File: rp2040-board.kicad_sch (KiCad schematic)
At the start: 95 parts, among them J1 24V IN, J10 E0-RUNOUT, J11 FAN0, J12 FAN1, J13 FAN2, J14 HB, J15 E0, J16 TH-E0, J2 USB4105-GF-A, J22 Exp. Header 2, J23 Exp. Header 3, J3 PGA2040, J4 Exp. Header 1, J5 PROBE, J6 X-ENDSTOP, J7 TH-HB, J8 Y-ENDSTOP, J9 Z-ENDSTOP, Q1 AO3400C, Q2 AO3400C, Q3 AO3400C, U1 AMS1117-3.3, U2 TPS5450DDAR, U3 74HCT365D,653, U4 FDS8896, U5 FDS8896

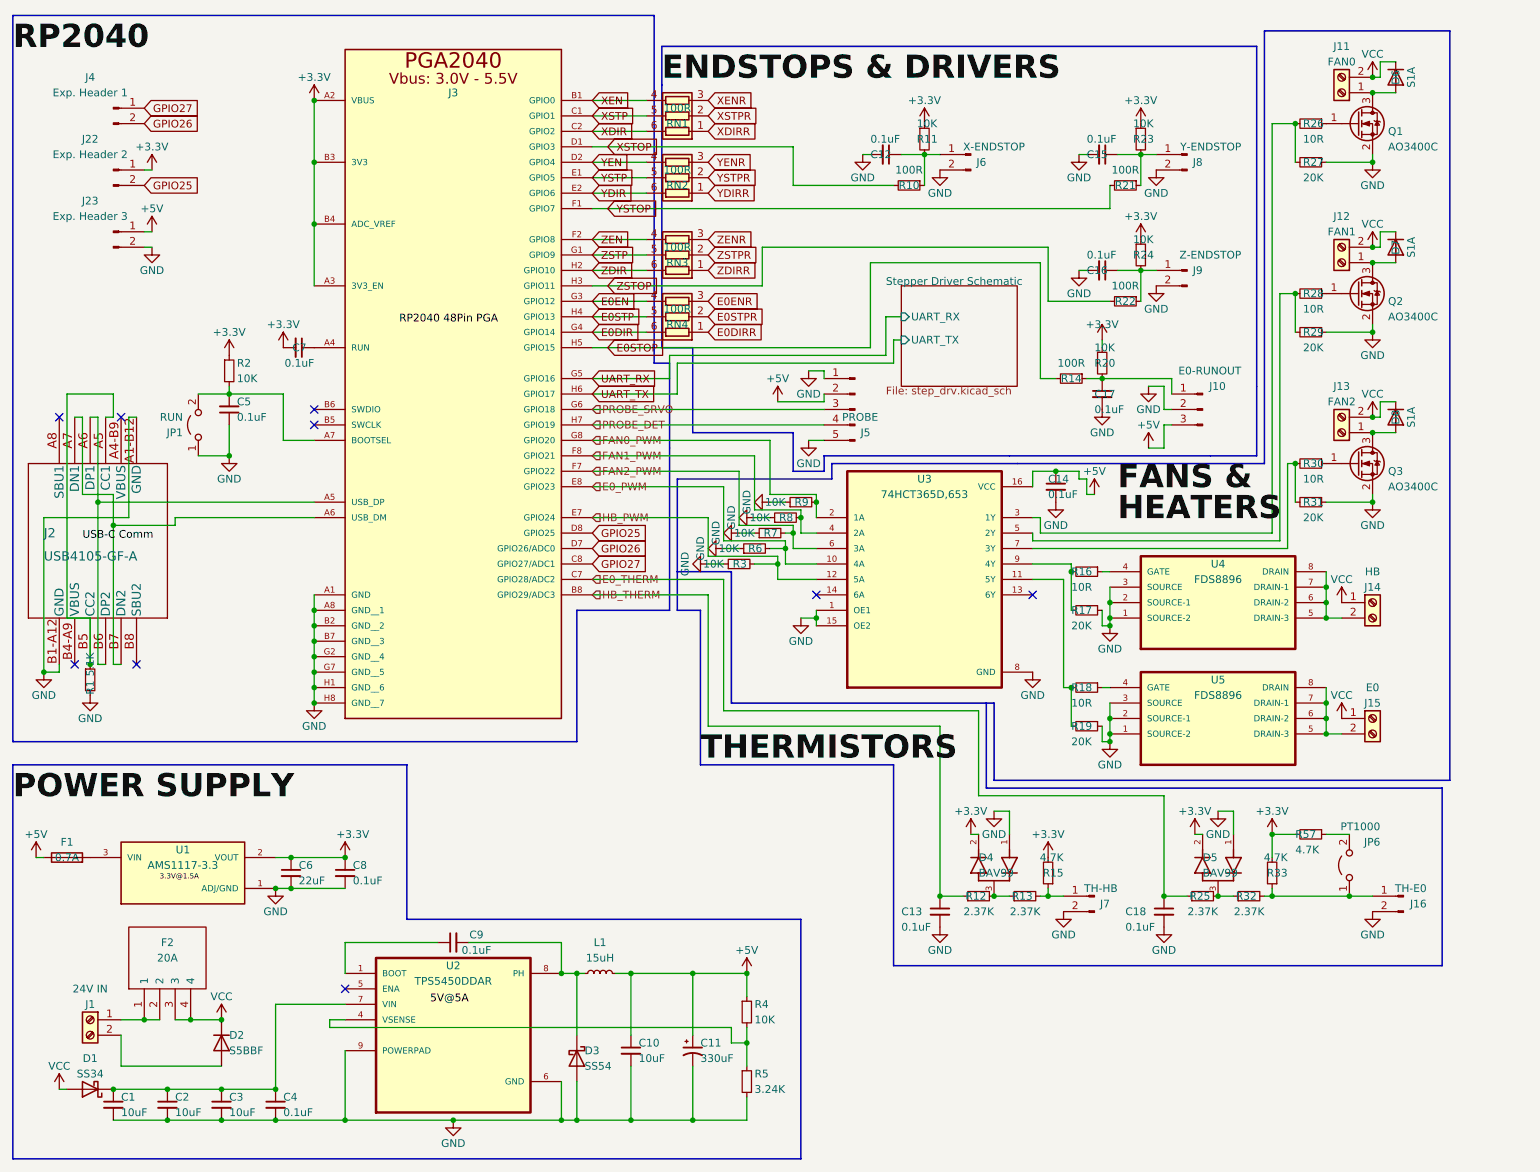
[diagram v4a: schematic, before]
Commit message: Big updates, start of V2, actual RP2040
change from V1.2 to V2 because of many optimizations to come
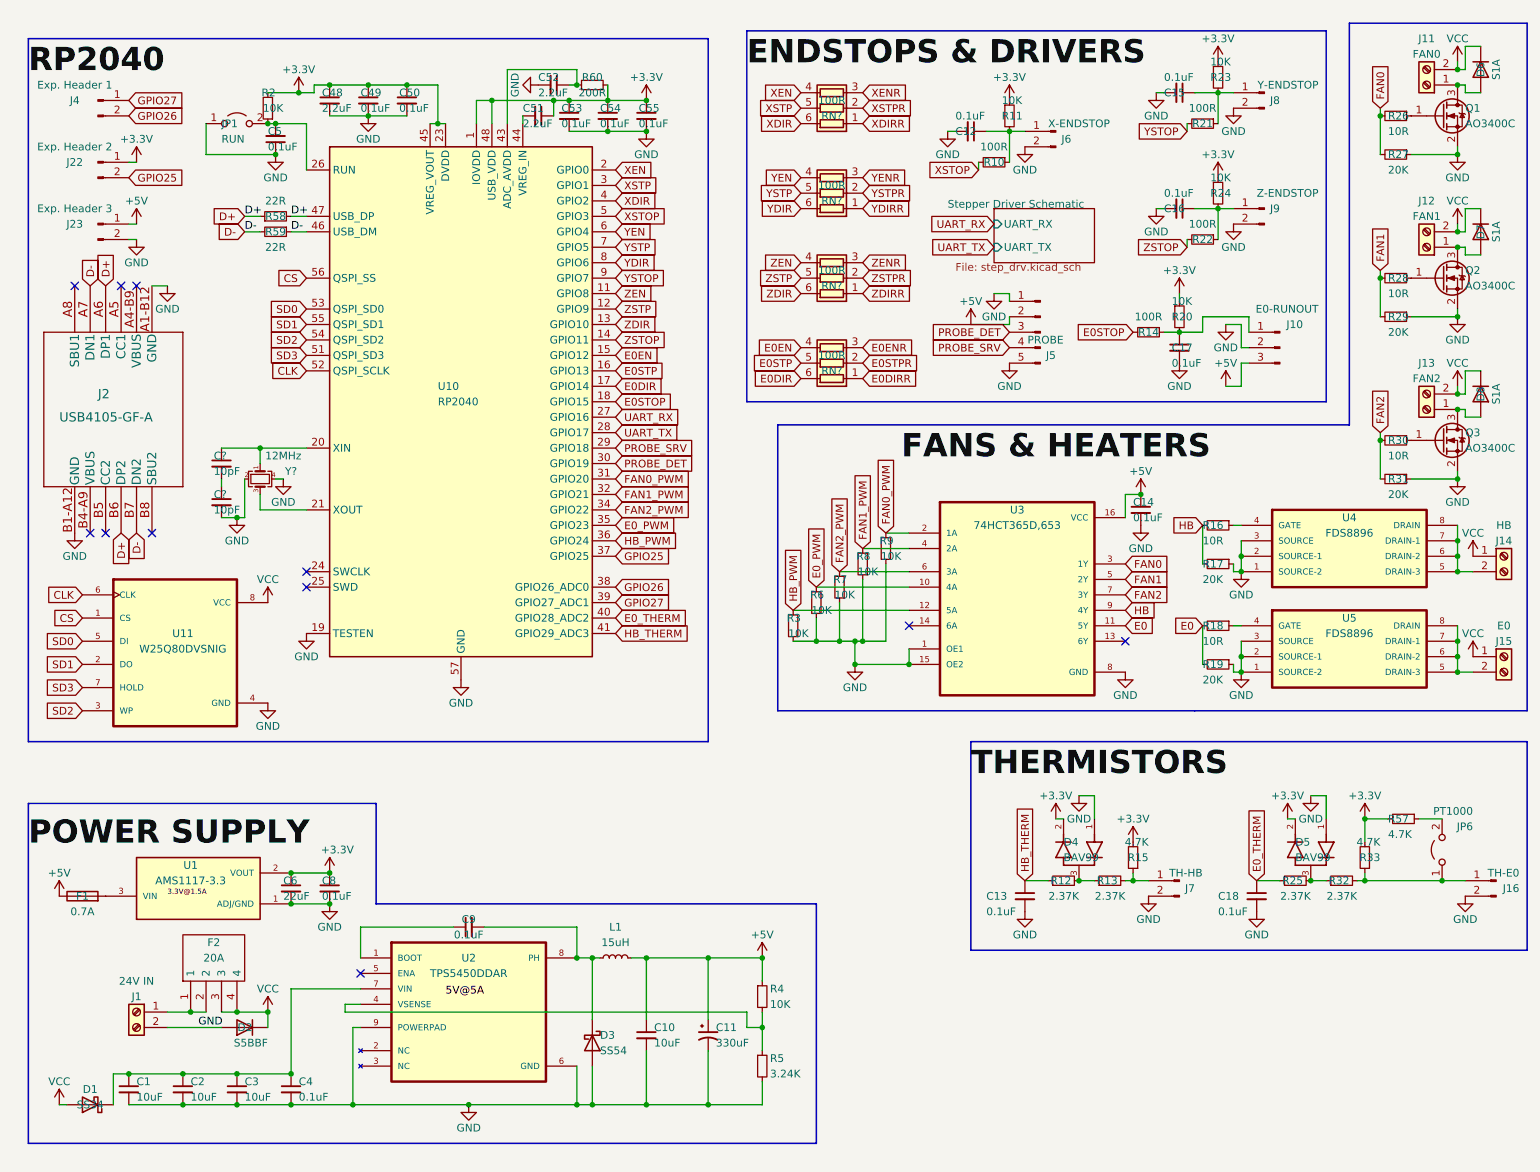
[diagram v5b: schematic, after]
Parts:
- removed C7: 0.1uF, Capacitor_SMD:C_0805_2012Metric_Pad1.18x1.45mm, symbol Device:C_Small
- removed J3: PGA2040, PGA2040:PGA2040_PTH_NO_SLOT, symbol PGA2040:PGA2040
- removed R1: 5.1K, Resistor_SMD:R_0805_2012Metric_Pad1.20x1.40mm, symbol Device:R_Small
- removed RN1, RN2, RN3, RN4: 100R, Resistor_SMD:R_Array_Convex_4x0603, symbol Device:R_Pack03
- added C48, C51, C52: 2.2uF, Capacitor_SMD:C_0805_2012Metric, symbol Device:C_Small
- added C49, C50, C53, C54, C55: 0.1uF, Capacitor_SMD:C_0805_2012Metric, symbol Device:C_Small
- added C? (x2): 10pF, Capacitor_SMD:C_0805_2012Metric, symbol Device:C_Small
- added R58, R59: 22R, Resistor_SMD:R_0805_2012Metric, symbol Device:R_Small
- added R60: 200R, Capacitor_SMD:C_0805_2012Metric, symbol Device:R_Small
- added RN? (x4): 100R, Resistor_SMD:R_Array_Convex_4x0603, symbol Device:R_Pack03
- added U10: RP2040, Package_DFN_QFN:QFN-56-1EP_7x7mm_P0.4mm_EP3.2x3.2mm, symbol MCU_RaspberryPi:RP2040
- added U11: W25Q80DVSNIG, SOIC127P600X175-8N, symbol W25Q80DVSNIG_TR:W25Q80DVSNIG_TR
- added Y?: 12MHz, Oscillator:Oscillator_SMD_SeikoEpson_SG8002CE-4Pin_3.2x2.5mm, symbol Device:Crystal_GND24_Small
- C1, C10, C12, C13, C14, C15, C16, C17, C18, C2, C3, C4, C5, C6, C8, C9: footprint Capacitor_SMD:C_0805_2012Metric_Pad1.18x1.45mm -> Capacitor_SMD:C_0805_2012Metric
- F1: footprint Fuse:Fuse_1812_4532Metric_Pad1.30x3.40mm -> Fuse:Fuse_1812_4532Metric
- L1: footprint Inductor_SMD:L_1210_3225Metric_Pad1.42x2.65mm -> Inductor_SMD:L_1210_3225Metric
- R10, R11, R12, R13, R14, R15, R16, R17, R18, R19, R2, R20, R21, R22, R23, R24, R25, R26, R27, R28, R29, R3, R30, R31, R32, R33, R4, R5, R57, R6, R7, R8, R9: footprint Resistor_SMD:R_0805_2012Metric_Pad1.20x1.40mm -> Resistor_SMD:R_0805_2012Metric
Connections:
- net PROBE_SRVO is gone; now on net PROBE_DET: J5.3 (Pin_3)
- net +3.3V: now also R2.2, C48.1, C49.1, C50.1, C51.1, C53.1, C54.1, C55.1, R60.2, U10.1 (IOVDD), U10.10 (IOVDD), U10.22 (IOVDD), U10.23 (DVDD), U10.33 (IOVDD), U10.42 (IOVDD), U10.45 (VREG_VOUT), U10.48 (USB_VDD), U10.49 (IOVDD), U10.50 (DVDD); no longer R2.1
- net E0DIR: now also RN?.6 (R1.2), U10.17 (GPIO14)
- net E0DIRR: now also RN?.1 (R1.1)
- net E0EN: now also RN?.4 (R3.2), U10.15 (GPIO12)
- net E0ENR: now also RN?.3 (R3.1)
- net E0STOP: now also U10.18 (GPIO15)
- net E0STP: now also RN?.5 (R2.2), U10.16 (GPIO13)
- net E0STPR: now also RN?.2 (R2.1)
- net E0_PWM: now also U10.35 (GPIO23)
- net E0_THERM: now also U10.40 (GPIO28_ADC2)
- net FAN0_PWM: now also U10.31 (GPIO20)
- net FAN1_PWM: now also U10.32 (GPIO21)
- net FAN2_PWM: now also U10.34 (GPIO22)
- net GND: now also D2.1 (A), J1.2 (Pin_2), C48.2, C49.2, C50.2, C52.2, C53.2, C54.2, C55.2, C?.2, U10.19 (TESTEN), U10.57 (GND), U11.4 (GND), Y?.2, Y?.4
- net GPIO25: now also U10.37 (GPIO25)
- net GPIO26: now also U10.38 (GPIO26_ADC0)
- net GPIO27: now also U10.39 (GPIO27_ADC1)
- net HB_PWM: now also U10.36 (GPIO24)
- net HB_THERM: now also U10.41 (GPIO29_ADC3)
- net PROBE_DET: now also U10.30 (GPIO19); no longer J5.4 (Pin_4)
- net UART_RX: now also U10.27 (GPIO16)
- net UART_TX: now also U10.28 (GPIO17)
- net VCC: now also U11.8 (VCC)
- net XDIR: now also RN?.6 (R1.2), U10.4 (GPIO2)
- net XDIRR: now also RN?.1 (R1.1)
- net XEN: now also RN?.4 (R3.2), U10.2 (GPIO0)
- net XENR: now also RN?.3 (R3.1)
- net XSTOP: now also U10.5 (GPIO3)
- net XSTP: now also RN?.5 (R2.2), U10.3 (GPIO1)
- net XSTPR: now also RN?.2 (R2.1)
- net YDIR: now also RN?.6 (R1.2), U10.8 (GPIO6)
- net YDIRR: now also RN?.1 (R1.1)
- net YEN: now also RN?.4 (R3.2), U10.6 (GPIO4)
- net YENR: now also RN?.3 (R3.1)
- net YSTOP: now also U10.9 (GPIO7)
- net YSTP: now also RN?.5 (R2.2), U10.7 (GPIO5)
- net YSTPR: now also RN?.2 (R2.1)
- net ZDIR: now also RN?.6 (R1.2), U10.13 (GPIO10)
- net ZDIRR: now also RN?.1 (R1.1)
- net ZEN: now also RN?.4 (R3.2), U10.11 (GPIO8)
- net ZENR: now also RN?.3 (R3.1)
- net ZSTOP: now also U10.14 (GPIO11)
- net ZSTP: now also RN?.5 (R2.2), U10.12 (GPIO9)
- net ZSTPR: now also RN?.2 (R2.1)
- net E0: now reaches R18.2, R19.2, U3.11 (5Y)
- net at C5.2, JP1.2 (B): now also R2.1, U10.26 (RUN); no longer R2.2
- net FAN0: now reaches R26.2, R27.2, U3.3 (1Y)
- net HB: now reaches R16.2, R17.2, U3.9 (4Y)
- net FAN1: now reaches R28.2, R29.2, U3.5 (2Y)
- net at J2.A5 (CC1): no longer J2.B5 (CC2)
- net D+: now reaches J2.A6 (DP1), J2.B6 (DP2)
- net D+: now also R58.1, R58.2, U10.47 (USB_DP)
- net D-: now reaches J2.A7 (DN1), J2.B7 (DN2)
- net D-: now also R59.1, R59.2, U10.46 (USB_DM)
- net FAN2: now reaches R30.2, R31.2, U3.7 (3Y)
- new net: C?.1, U10.20 (XIN), Y?.1
- new net: U10.21 (XOUT), Y?.3
- new net: C52.1, R60.1, U10.43 (ADC_AVDD)
- new net: C51.2, U10.44 (VREG_IN)
- new net: C?.1, C?.2
- new net CLK: U10.52 (QSPI_SCLK), U11.6 (CLK)
- new net CS: U10.56 (QSPI_SS), U11.1 (CS)
- new net PROBE_SRV: J5.4 (Pin_4), U10.29 (GPIO18)
- new net SD0: U10.53 (QSPI_SD0), U11.5 (DI)
- new net SD1: U10.55 (QSPI_SD1), U11.2 (DO)
- new net SD2: U10.54 (QSPI_SD2), U11.3 (WP)
- new net SD3: U10.51 (QSPI_SD3), U11.7 (HOLD)
- no-connect marks 9 -> 11
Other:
- title: RP2040 Board -> FriedSalmon2040
- moved on the sheet: C1, C10, C11, C12, C13, C14, C15, C16, C17, C18, C2, C3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

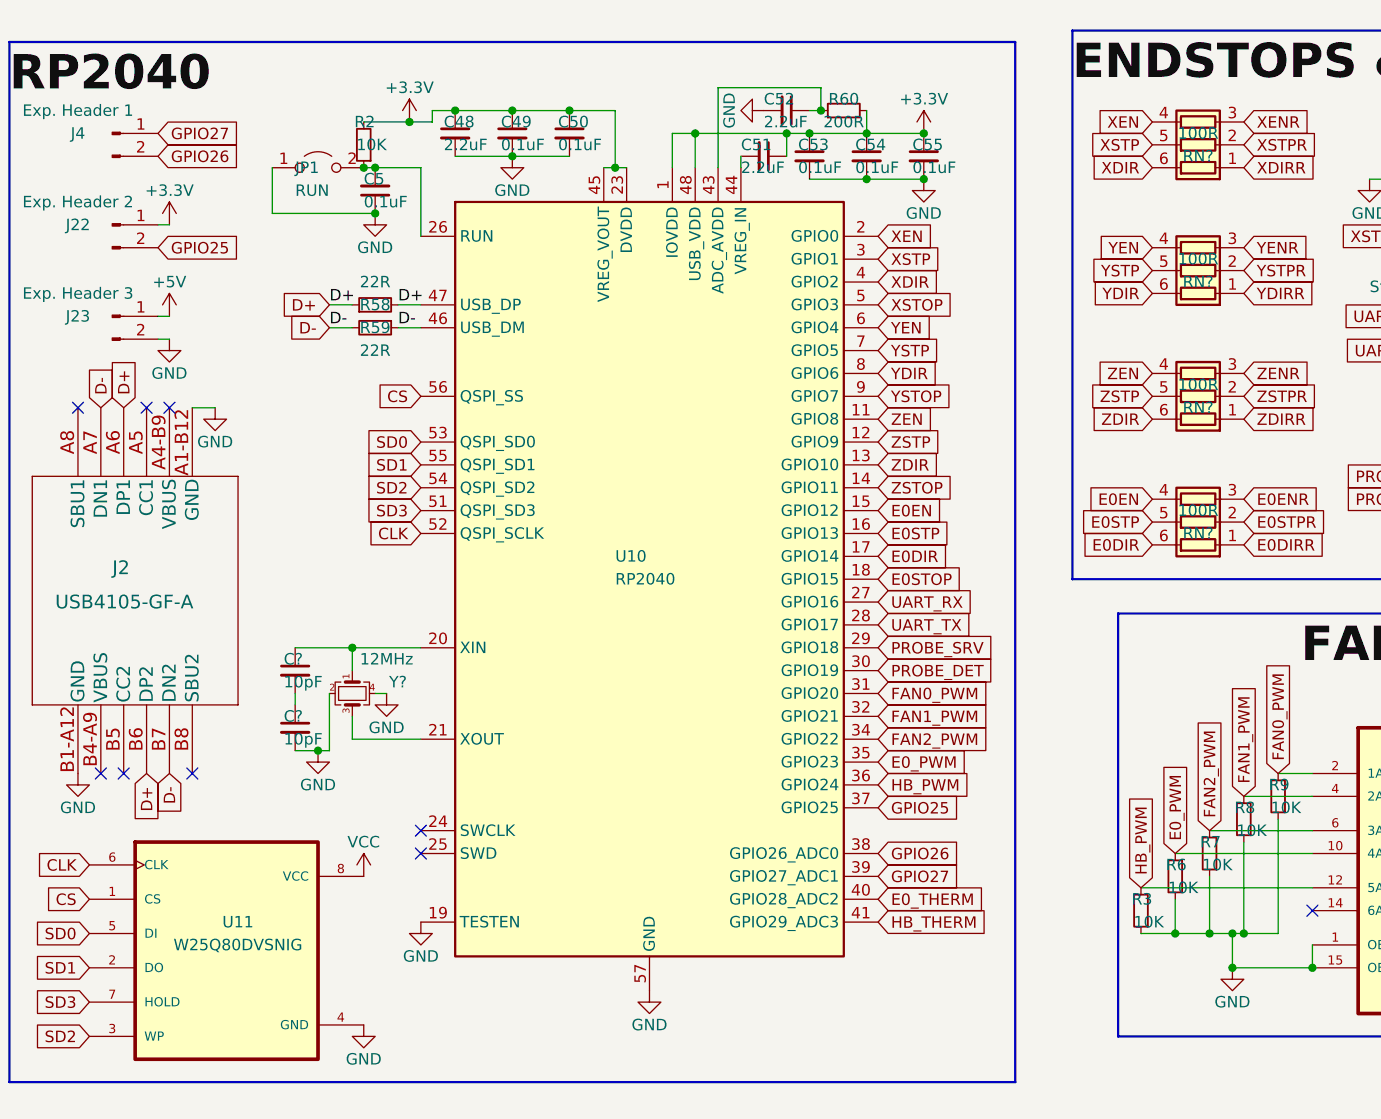
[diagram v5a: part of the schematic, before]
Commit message: Updates, Move to 0602, Optimize Routing
* 0805 -> 0602
* Flash 8MB SOIC8 -> Flash 16MB USON 2x3
* Indev Pic
* Trace Optimization
* Whatever else i forgor
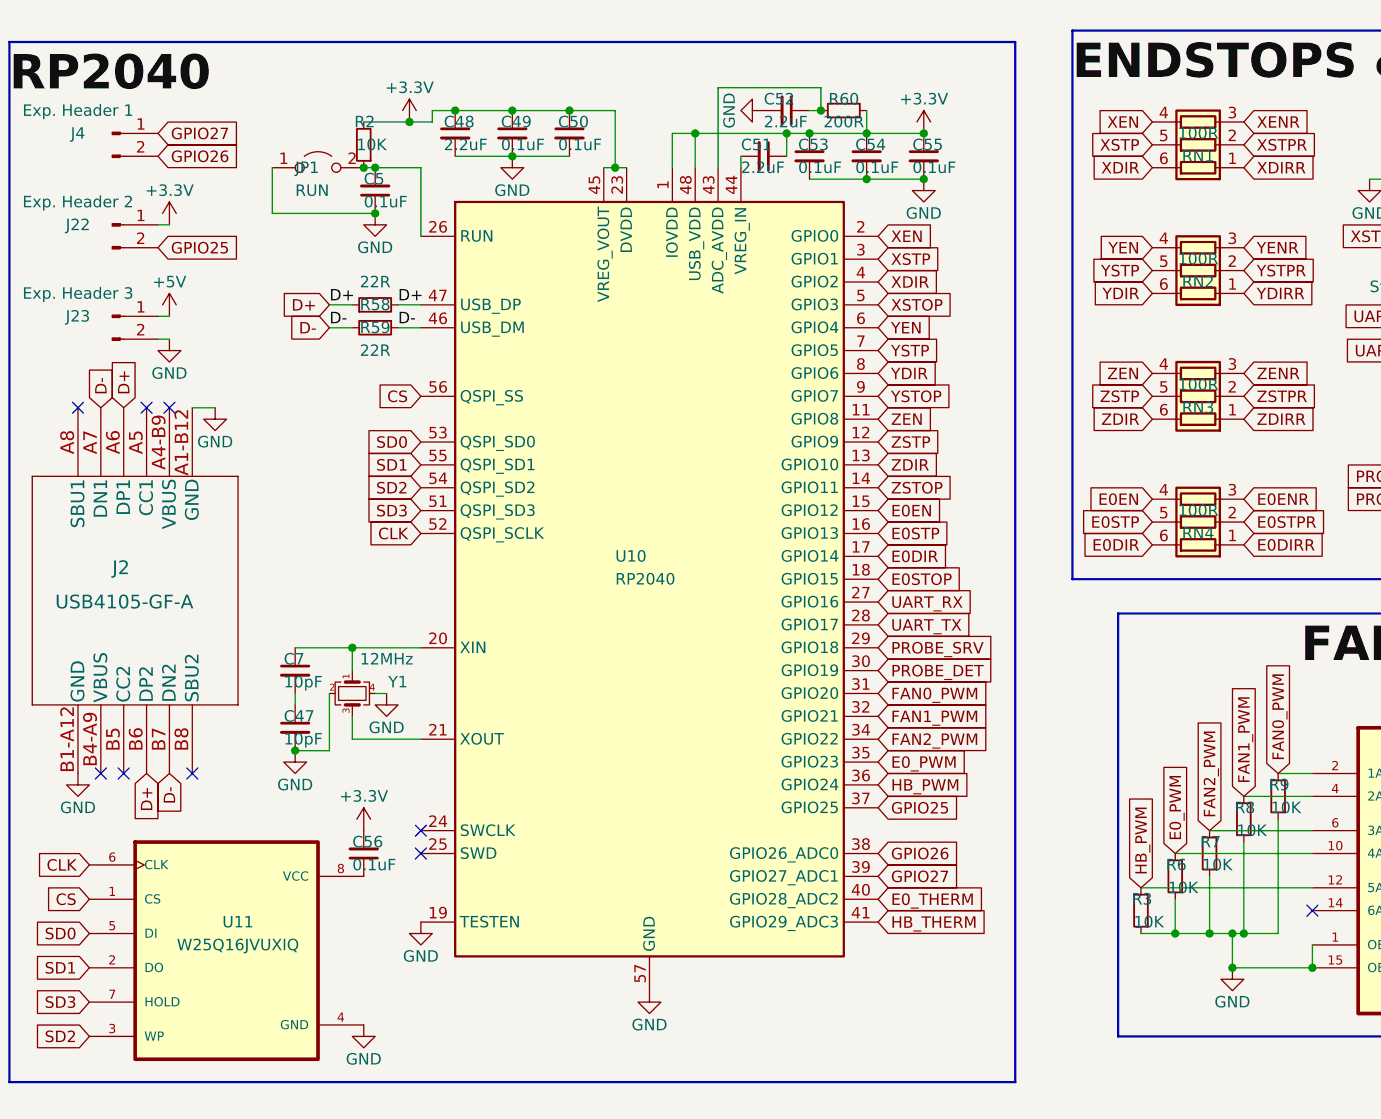
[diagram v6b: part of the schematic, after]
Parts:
- added C56: 0.1uF, Capacitor_SMD:C_0603_1608Metric, symbol Device:C_Small
- C1, C10, C12, C13, C14, C15, C16, C17, C18, C2, C3, C4, C48, C5, C51, C52, C8, C9: footprint Capacitor_SMD:C_0805_2012Metric -> Capacitor_SMD:C_0603_1608Metric
- C47, C7: renamed from C?; footprint Capacitor_SMD:C_0805_2012Metric -> Capacitor_SMD:C_0603_1608Metric
- C49, C50, C53, C54, C55: footprint Capacitor_SMD:C_0805_2012Metric -> Capacitor_SMD:C_0603_1608Metric; MANUFACTURER (none) -> Samsung Electro Mechanics
- D6, D7, D8: MANUFACTURER (none) -> onsemi
- R10, R11, R12, R13, R14, R15, R16, R17, R18, R19, R2, R20, R21, R22, R23, R24, R25, R26, R27, R28, R29, R3, R30, R31, R32, R33, R4, R5, R57, R58, R59, R6, R7, R8, R9: footprint Resistor_SMD:R_0805_2012Metric -> Resistor_SMD:R_0603_1608Metric
- R60: footprint Capacitor_SMD:C_0805_2012Metric -> Resistor_SMD:R_0603_1608Metric
- U11: value W25Q80DVSNIG -> W25Q16JVUXIQ; footprint SOIC127P600X175-8N -> W25Q16JVUXIQ:SON50P300X200X60-9N
- gave numbers to parts that had none: 5
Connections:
- net +3.3V: now also C56.2
- net VCC: no longer U11.8 (VCC)
- new net: C56.1, U11.8 (VCC)
